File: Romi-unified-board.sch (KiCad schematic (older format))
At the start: 67 parts, among them J1 ServoAnalog, J10 LIDAR_DATA, J11 LIDAR_MOTOR, J12 ROMI-Encoder, J13 ROMI-Encoder, J14 THING, J15 THING, J2 Conn_01x19_Female, J3 LineSensor, J4 LineSensor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

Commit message: Re-routed board
Resolved issues #6  and #5
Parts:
- removed JP1: Jumper_3_Bridged12, Jumper:SolderJumper-3_P1.3mm_Bridged12_RoundedPad1.0x1.5mm, symbol Jumper:Jumper_3_Bridged12
- added SW2: SW_SPDT, unified:CSS-1210TB, symbol Switch:SW_SPDT
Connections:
- wire segments 277 -> 274
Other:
- moved on the sheet: H1
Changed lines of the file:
@@
 Text Notes 12250 5350 0    50   ~ 0
 ML-
-Text GLabel 4650 2050 2    50   Input ~ 0
+Text GLabel 4650 2350 2    50   Input ~ 0
 GPIO21
-Text GLabel 4650 2150 2    50   Input ~ 0
+Text GLabel 4650 2450 2    50   Input ~ 0
 GPIO17
-Text GLabel 4650 2250 2    50   Input ~ 0
+Text GLabel 4650 2550 2    50   Input ~ 0
 GPIO16
-Text GLabel 4650 2350 2    50   Input ~ 0
+Text GLabel 4650 2650 2    50   Input ~ 0
 GPIO19
-Text GLabel 4650 2450 2    50   Input ~ 0
+Text GLabel 4650 2750 2    50   Input ~ 0
 GPIO18
-Text GLabel 4650 2550 2    50   Input ~ 0
+Text GLabel 4650 2850 2    50   Input ~ 0
 GPIO5
-Text GLabel 4650 2650 2    50   Input ~ 0
+Text GLabel 4650 2950 2    50   Input ~ 0
 GPIO4
-Text GLabel 4650 2750 2    50   Input ~ 0
+Text GLabel 4650 3050 2    50   Input ~ 0
 GPIO36
-Text GLabel 4650 2850 2    50   Input ~ 0
+Text GLabel 4650 3150 2    50   Input ~ 0
 GPIO39
-Text GLabel 4650 2950 2    50   Input ~ 0
+Text GLabel 4650 3250 2    50   Input ~ 0
 GPIO34
-Text GLabel 4650 3050 2    50   Input ~ 0
+Text GLabel 4650 3350 2    50   Input ~ 0
 GPIO25
-Text GLabel 4650 3150 2    50   Input ~ 0
+Text GLabel 4650 3450 2    50   Input ~ 0
 GPIO26
 $Comp
 L power:GND #PWR0110
 U 1 1 5EEB6068
-P 4950 3250
-F 0 "#PWR0110" H 4950 3000 50  0001 C CNN
-F 1 "GND" V 4955 3122 50  0000 R CNN
-F 2 "" H 4950 3250 50  0001 C CNN
-F 3 "" H 4950 3250 50  0001 C CNN
-	1    4950 3250
+P 4950 3550
+F 0 "#PWR0110" H 4950 3300 50  0001 C CNN
+F 1 "GND" V 4955 3422 50  0000 R CNN
+F 2 "" H 4950 3550 50  0001 C CNN
+F 3 "" H 4950 3550 50  0001 C CNN
+	1    4950 3550
 	0    -1   -1   0
 $EndComp
@@
 L power:+3.3V #PWR0111
 U 1 1 5EEB70F6
-P 4950 3450
-F 0 "#PWR0111" H 4950 3300 50  0001 C CNN
-F 1 "+3.3V" V 4965 3578 50  0000 L CNN
-F 2 "" H 4950 3450 50  0001 C CNN
-F 3 "" H 4950 3450 50  0001 C CNN
-	1    4950 3450
+P 4950 3750
+F 0 "#PWR0111" H 4950 3600 50  0001 C CNN
+F 1 "+3.3V" V 4965 3878 50  0000 L CNN
+F 2 "" H 4950 3750 50  0001 C CNN
+F 3 "" H 4950 3750 50  0001 C CNN
+	1    4950 3750
 	0    1    1    0
 $EndComp
@@
 	2650 2850 2550 2850
 Wire Wire Line
-	4550 2050 4650 2050
-Wire Wire Line
-	4550 2150 4650 2150
-Wire Wire Line
-	4550 2250 4650 2250
-Wire Wire Line
 	4550 2350 4650 2350
 Wire Wire Line
@@
 	4550 3150 4650 3150
 Wire Wire Line
-	4950 3250 4550 3250
-Wire Wire Line
-	4550 3450 4950 3450
+	4550 3250 4650 3250
+Wire Wire Line
+	4550 3350 4650 3350
+Wire Wire Line
+	4550 3450 4650 3450
+Wire Wire Line
+	4950 3550 4550 3550
+Wire Wire Line
+	4550 3750 4950 3750
 $Comp
 L power:GND #PWR0113
@@
 Wire Wire Line
 	6300 1300 6350 1300
-$Comp
-L Mechanical:MountingHole H1
-U 1 1 5EF4C315
-P 5200 3850
-F 0 "H1" H 5300 3896 50  0000 L CNN
-F 1 "MountingHole" H 5300 3805 50  0000 L CNN
-F 2 "MountingHole:MountingHole_2.2mm_M2_DIN965" H 5200 3850 50  0001 C CNN
-F 3 "~" H 5200 3850 50  0001 C CNN
-	1    5200 3850
-	1    0    0    -1
-$EndComp
 $Comp
 L Mechanical:MountingHole H2
@@
 NoConn ~ 1250 2450
 NoConn ~ 2150 2550
-NoConn ~ 5050 2950
+NoConn ~ 5050 3250
 NoConn ~ 1250 2250
 NoConn ~ 1250 2300
-NoConn ~ 5050 2750
-NoConn ~ 5050 2850
+NoConn ~ 5050 3050
+NoConn ~ 5050 3150
 NoConn ~ 2150 2250
 NoConn ~ 2150 2350
@@
 NoConn ~ 3550 3050
 NoConn ~ 3550 3150
-NoConn ~ 5050 2150
-NoConn ~ 5050 2250
+NoConn ~ 5050 2450
+NoConn ~ 5050 2550
 NoConn ~ 1250 3050
 NoConn ~ 1250 2950
 NoConn ~ 2150 2650
-NoConn ~ 5050 3150
-NoConn ~ 5050 2650
+NoConn ~ 5050 3450
+NoConn ~ 5050 2950
 NoConn ~ 2150 2850
 NoConn ~ 3550 3250
-NoConn ~ 5050 3050
+NoConn ~ 5050 3350
 NoConn ~ 2150 2750
 NoConn ~ 3550 3550
@@
 Text Notes 8650 2900 0    50   ~ 0
 Free: 23 22 21 19 18 5
-Text GLabel 3200 6550 0    50   Input ~ 0
+Text GLabel 3650 7050 2    50   Input ~ 0
 GPIO23
-Text GLabel 3800 6550 2    50   Input ~ 0
+Text GLabel 3650 7250 2    50   Input ~ 0
 GPIO21
 $Comp
@@
 Wire Wire Line
 	6000 -850 6000 -800
-$Comp
-L Jumper:Jumper_3_Bridged12 JP1
-U 1 1 5F229CDD
-P 3500 6550
-F 0 "JP1" H 3500 6754 50  0000 C CNN
-F 1 "Jumper_3_Bridged12" H 3500 6663 50  0000 C CNN
-F 2 "Jumper:SolderJumper-3_P1.3mm_Bridged12_RoundedPad1.0x1.5mm" H 3500 6550 50  0001 C CNN
-F 3 "~" H 3500 6550 50  0001 C CNN
-	1    3500 6550
-	-1   0    0    1
-$EndComp
-Wire Wire Line
-	3800 6550 3750 6550
-Wire Wire Line
-	3500 6700 3500 6750
-Wire Wire Line
-	3250 6550 3200 6550
 Text GLabel 6350 1000 2    50   Input ~ 0
 GPIO23
 Text GLabel 8000 1300 2    50   Input ~ 0
 SDA
-Text GLabel 3500 6400 1    50   Input ~ 0
+Text GLabel 3250 7150 0    50   Input ~ 0
 SDA
 $Comp
@@
 Wire Wire Line
 	6400 2650 6300 2650
+$Comp
+L Mechanical:MountingHole H1
+U 1 1 5EF4C315
+P 5550 4000
+F 0 "H1" H 5650 4046 50  0000 L CNN
+F 1 "MountingHole" H 5750 3900 50  0000 L CNN
+F 2 "MountingHole:MountingHole_2.2mm_M2_DIN965" H 5550 4000 50  0001 C CNN
+F 3 "~" H 5550 4000 50  0001 C CNN
+	1    5550 4000
+	1    0    0    -1
+$EndComp
+$Comp
+L Switch:SW_SPDT SW2
+U 1 1 5F890447
+P 3450 7150
+F 0 "SW2" H 3450 7435 50  0000 C CNN
+F 1 "SW_SPDT" H 3450 7344 50  0000 C CNN
+F 2 "unified:CSS-1210TB" H 3450 7150 50  0001 C CNN
+F 3 "~" H 3450 7150 50  0001 C CNN
+	1    3450 7150
+	1    0    0    -1
+$EndComp
 $EndSCHEMATC

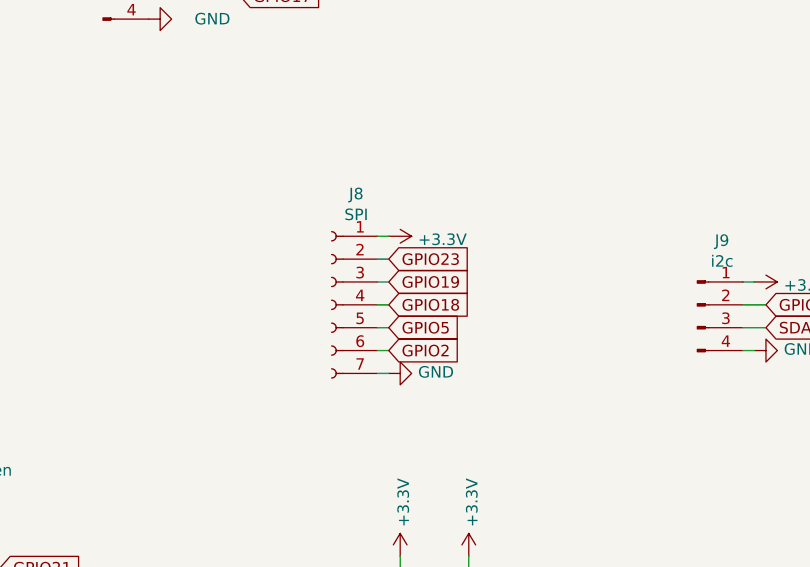
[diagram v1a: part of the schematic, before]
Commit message: flipped ultrasonic, removed IO2 from j8
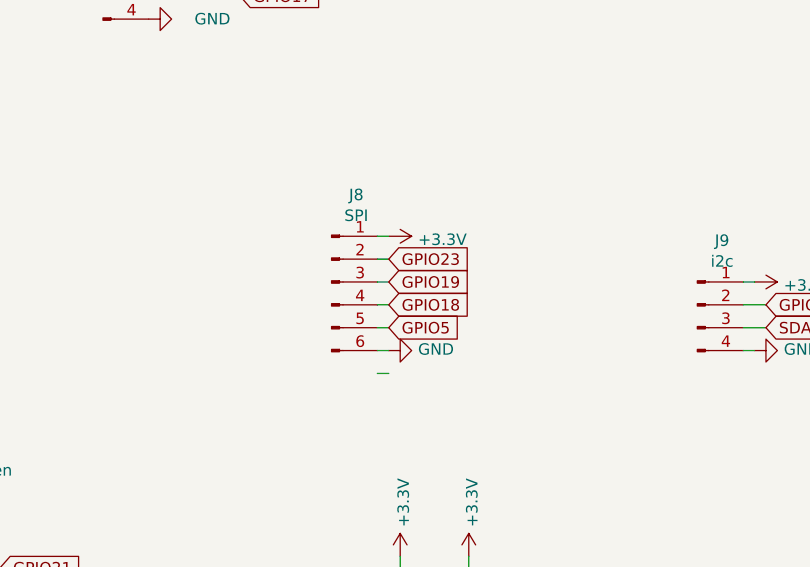
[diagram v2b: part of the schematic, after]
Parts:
- removed J8: SPI, Connector_PinSocket_2.54mm:PinSocket_1x07_P2.54mm_Vertical, symbol Connector:Conn_01x07_Female
- added J8: SPI, Connector_PinSocket_2.54mm:PinSocket_1x06_P2.54mm_Vertical, symbol Connector:Conn_01x06_Male
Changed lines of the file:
@@
 L power:GND #PWR0123
 U 1 1 5EEAECD4
-P 6350 1500
-F 0 "#PWR0123" H 6350 1250 50  0001 C CNN
-F 1 "GND" V 6355 1372 50  0000 R CNN
-F 2 "" H 6350 1500 50  0001 C CNN
-F 3 "" H 6350 1500 50  0001 C CNN
-	1    6350 1500
+P 6350 1400
+F 0 "#PWR0123" H 6350 1150 50  0001 C CNN
+F 1 "GND" V 6355 1272 50  0000 R CNN
+F 2 "" H 6350 1400 50  0001 C CNN
+F 3 "" H 6350 1400 50  0001 C CNN
+	1    6350 1400
 	0    -1   -1   0
 $EndComp
@@
 Text GLabel 16750 2800 0    50   Input ~ 0
 GPIO15
-$Comp
-L Connector:Conn_01x07_Female J8
-U 1 1 5F79F56E
-P 6100 1200
-F 0 "J8" H 5992 1685 50  0000 C CNN
-F 1 "SPI" H 5992 1594 50  0000 C CNN
-F 2 "Connector_PinSocket_2.54mm:PinSocket_1x07_P2.54mm_Vertical" H 6100 1200 50  0001 C CNN
-F 3 "~" H 6100 1200 50  0001 C CNN
-	1    6100 1200
-	-1   0    0    -1
-$EndComp
-Text GLabel 6350 1400 2    50   Input ~ 0
-GPIO2
 Wire Wire Line
 	6350 1500 6300 1500
@@
 	1    0    0    -1
 $EndComp
+$Comp
+L Connector:Conn_01x06_Male J8
+U 1 1 5F879B4D
+P 6100 1100
+F 0 "J8" H 6208 1481 50  0000 C CNN
+F 1 "SPI" H 6208 1390 50  0000 C CNN
+F 2 "Connector_PinSocket_2.54mm:PinSocket_1x06_P2.54mm_Vertical" H 6100 1100 50  0001 C CNN
+F 3 "~" H 6100 1100 50  0001 C CNN
+	1    6100 1100
+	1    0    0    -1
+$EndComp

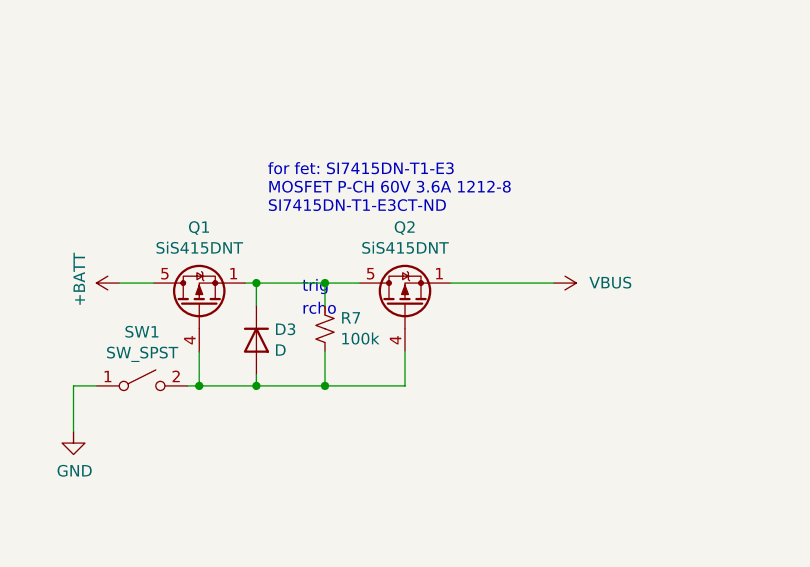
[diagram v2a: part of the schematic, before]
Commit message: Changes for rev2
rotated Q2
Fixed too-thin trace in DC-DC Circuit.
Created correct footprint for U1. No 9th pad.
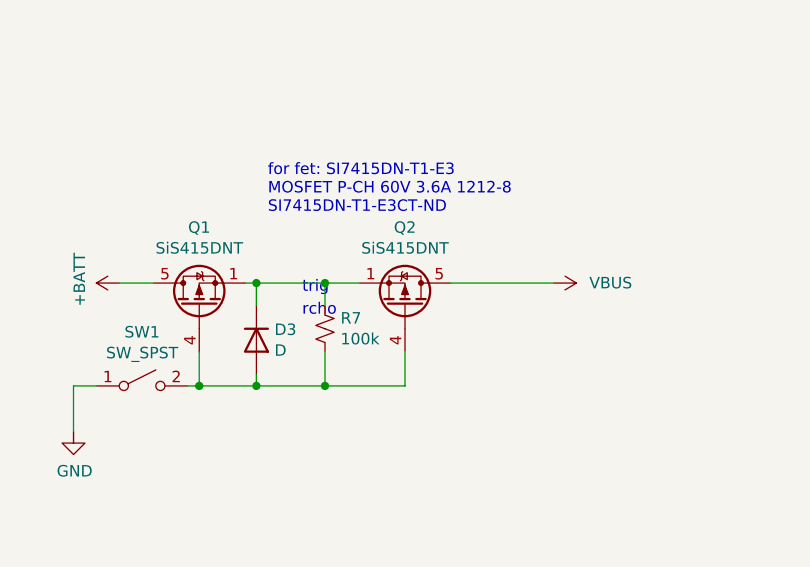
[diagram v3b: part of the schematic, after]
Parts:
- U1: footprint Package_DFN_QFN:DFN-8-1EP_3x3mm_P0.65mm_EP1.7x2.05mm -> unified:MP4423H
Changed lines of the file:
@@
 F 3 "https://www.vishay.com/docs/63684/sis415dnt.pdf" V 9100 -1100 50  0001 L CNN
 	1    9100 -1100
-	0    -1   -1   0
+	0    1    -1   0
 $EndComp
 $Comp
@@
 F 0 "U1" H 7350 5565 50  0000 C CNN
 F 1 "MP4423H" H 7350 5474 50  0000 C CNN
-F 2 "Package_DFN_QFN:DFN-8-1EP_3x3mm_P0.65mm_EP1.7x2.05mm" H 7050 4250 50  0001 C CNN
+F 2 "unified:MP4423H" H 7050 4250 50  0001 C CNN
 F 3 "" H 7050 4250 50  0001 C CNN
 	1    7350 4900

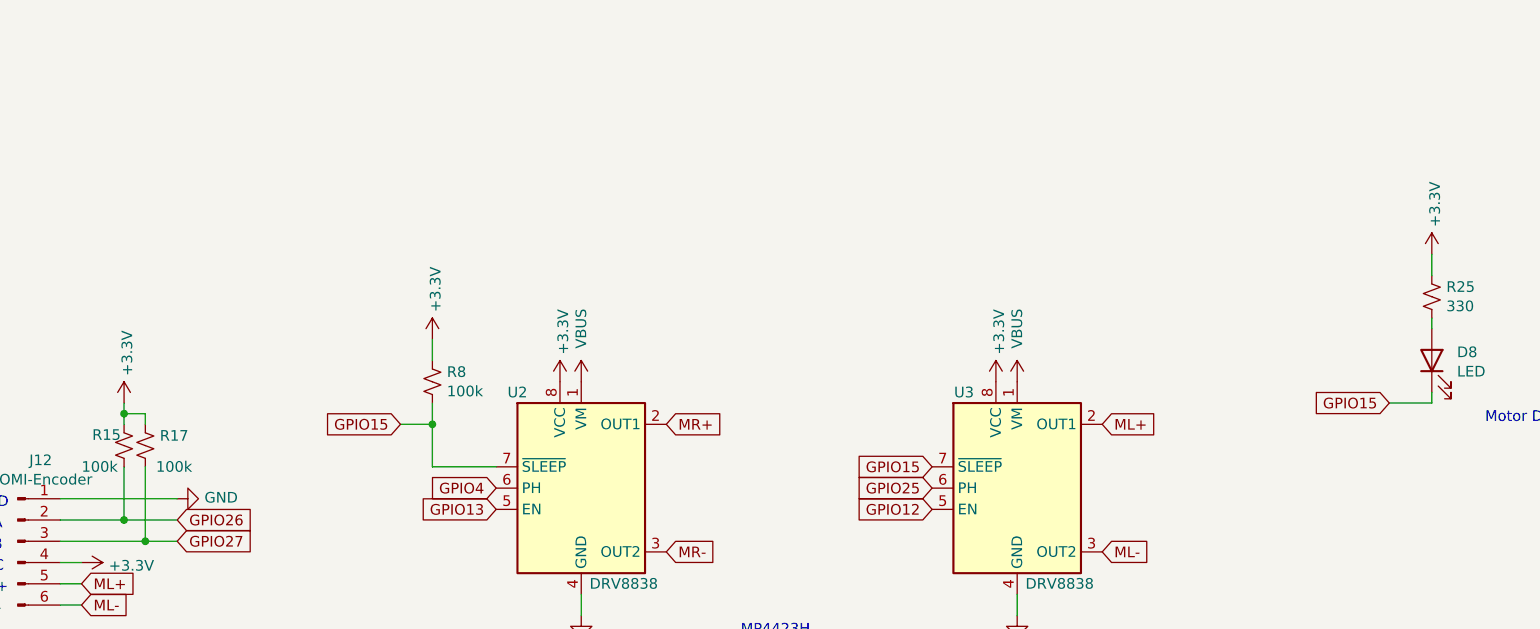
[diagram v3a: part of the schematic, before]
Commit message: Motor Disable is now a physical switch.
#7
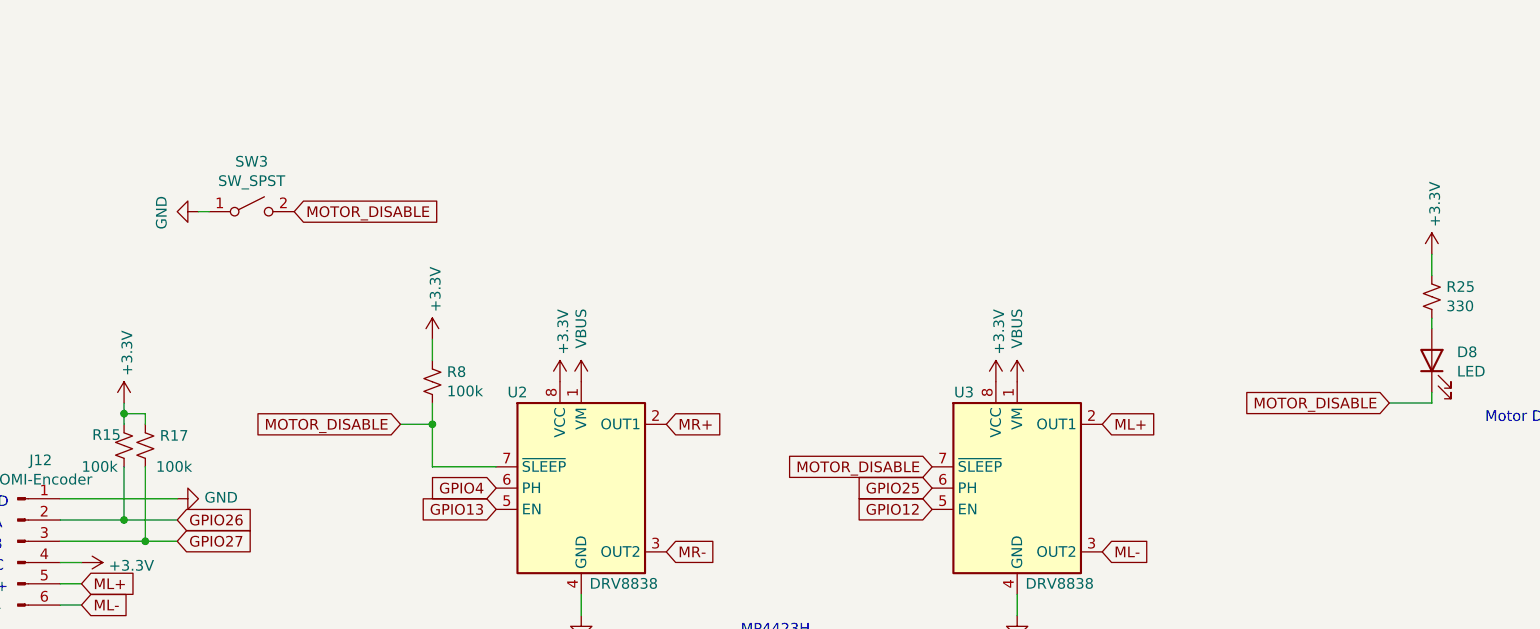
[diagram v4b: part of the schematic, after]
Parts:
- added SW3: SW_SPST, unified:CSS-1210TB, symbol Switch:SW_SPST
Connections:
- net labels added: MOTOR_DISABLE
- wire segments 274 -> 275
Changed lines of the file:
@@
 $EndComp
 Text GLabel 14250 2600 0    50   Input ~ 0
-GPIO15
+MOTOR_DISABLE
 Text GLabel 6350 1100 2    50   Input ~ 0
 GPIO19
@@
 	14400 2500 14400 2600
 Connection ~ 14400 2600
-Text GLabel 16750 2800 0    50   Input ~ 0
-GPIO15
 Wire Wire Line
 	6350 1500 6300 1500
@@
 Text Notes 17100 150  0    50   ~ 0
 DNP U5,U6,U7,U4
-Text GLabel 18900 2500 0    50   Input ~ 0
-GPIO15
 $Comp
 L Device:LED D8
@@
 	1    0    0    -1
 $EndComp
+Text GLabel 16750 2800 0    50   Input ~ 0
+MOTOR_DISABLE
+$Comp
+L Switch:SW_SPST SW3
+U 1 1 5F9B53FD
+P 13550 1600
+F 0 "SW3" H 13550 1835 50  0000 C CNN
+F 1 "SW_SPST" H 13550 1744 50  0000 C CNN
+F 2 "unified:CSS-1210TB" H 13550 1600 50  0001 C CNN
+F 3 "~" H 13550 1600 50  0001 C CNN
+	1    13550 1600
+	1    0    0    -1
+$EndComp
+Text GLabel 13750 1600 2    50   Input ~ 0
+MOTOR_DISABLE
+$Comp
+L power:GND #PWR0144
+U 1 1 5F9B5F0A
+P 13300 1600
+F 0 "#PWR0144" H 13300 1350 50  0001 C CNN
+F 1 "GND" H 13305 1427 50  0000 C CNN
+F 2 "" H 13300 1600 50  0001 C CNN
+F 3 "" H 13300 1600 50  0001 C CNN
+	1    13300 1600
+	0    1    1    0
+$EndComp
+Wire Wire Line
+	13350 1600 13300 1600
+Text GLabel 18900 2500 0    50   Input ~ 0
+MOTOR_DISABLE
 $EndSCHEMATC

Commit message: Rev2
Added smart servo connectors
Added IR sensor
Updated silk label
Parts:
- added C16, C17: 220u, Capacitor_SMD:CP_Elec_6.3x3.9, symbol Device:CP
- added J16, J17, J18: Conn_01x03_Male, Connector_JST:JST_PH_B3B-PH-K_1x03_P2.00mm_Vertical, symbol Connector:Conn_01x03_Male
- added U4: TSSP58038, OptoDevice:Vishay_MINICAST-3Pin, symbol Sensor_Proximity:TSSP58038
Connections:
- wire segments 275 -> 279
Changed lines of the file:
@@
 Text GLabel 18900 2500 0    50   Input ~ 0
 MOTOR_DISABLE
+$Comp
+L Connector:Conn_01x03_Male J16
+U 1 1 5F9C6157
+P 13550 450
+F 0 "J16" H 13658 731 50  0000 C CNN
+F 1 "Conn_01x03_Male" H 13658 640 50  0000 C CNN
+F 2 "Connector_JST:JST_PH_B3B-PH-K_1x03_P2.00mm_Vertical" H 13550 450 50  0001 C CNN
+F 3 "~" H 13550 450 50  0001 C CNN
+	1    13550 450
+	1    0    0    -1
+$EndComp
+$Comp
+L power:GND #PWR0147
+U 1 1 5F9C7080
+P 13750 350
+F 0 "#PWR0147" H 13750 100 50  0001 C CNN
+F 1 "GND" H 13755 177 50  0000 C CNN
+F 2 "" H 13750 350 50  0001 C CNN
+F 3 "" H 13750 350 50  0001 C CNN
+	1    13750 350
+	0    -1   -1   0
+$EndComp
+Text GLabel 13750 550  2    50   Input ~ 0
+GPIO33
+$Comp
+L power:VBUS #PWR0148
+U 1 1 5F9C76D4
+P 13750 450
+F 0 "#PWR0148" H 13750 300 50  0001 C CNN
+F 1 "VBUS" V 13750 700 50  0000 C CNN
+F 2 "" H 13750 450 50  0001 C CNN
+F 3 "" H 13750 450 50  0001 C CNN
+	1    13750 450
+	0    1    1    0
+$EndComp
+$Comp
+L Connector:Conn_01x03_Male J17
+U 1 1 5F9C9712
+P 14400 450
+F 0 "J17" H 14508 731 50  0000 C CNN
+F 1 "Conn_01x03_Male" H 14508 640 50  0000 C CNN
+F 2 "Connector_JST:JST_PH_B3B-PH-K_1x03_P2.00mm_Vertical" H 14400 450 50  0001 C CNN
+F 3 "~" H 14400 450 50  0001 C CNN
+	1    14400 450
+	1    0    0    -1
+$EndComp
+$Comp
+L power:GND #PWR0149
+U 1 1 5F9C9718
+P 14600 350
+F 0 "#PWR0149" H 14600 100 50  0001 C CNN
+F 1 "GND" H 14605 177 50  0000 C CNN
+F 2 "" H 14600 350 50  0001 C CNN
+F 3 "" H 14600 350 50  0001 C CNN
+	1    14600 350
+	0    -1   -1   0
+$EndComp
+Text GLabel 14600 550  2    50   Input ~ 0
+GPIO33
+$Comp
+L power:VBUS #PWR0150
+U 1 1 5F9C971F
+P 14600 450
+F 0 "#PWR0150" H 14600 300 50  0001 C CNN
+F 1 "VBUS" V 14600 700 50  0000 C CNN
+F 2 "" H 14600 450 50  0001 C CNN
+F 3 "" H 14600 450 50  0001 C CNN
+	1    14600 450
+	0    1    1    0
+$EndComp
+$Comp
+L Connector:Conn_01x03_Male J18
+U 1 1 5F9E0D75
+P 15200 450
+F 0 "J18" H 15308 731 50  0000 C CNN
+F 1 "Conn_01x03_Male" H 15308 640 50  0000 C CNN
+F 2 "Connector_JST:JST_PH_B3B-PH-K_1x03_P2.00mm_Vertical" H 15200 450 50  0001 C CNN
+F 3 "~" H 15200 450 50  0001 C CNN
+	1    15200 450
+	1    0    0    -1
+$EndComp
+$Comp
+L power:GND #PWR0151
+U 1 1 5F9E0D7B
+P 15400 350
+F 0 "#PWR0151" H 15400 100 50  0001 C CNN
+F 1 "GND" H 15405 177 50  0000 C CNN
+F 2 "" H 15400 350 50  0001 C CNN
+F 3 "" H 15400 350 50  0001 C CNN
+	1    15400 350
+	0    -1   -1   0
+$EndComp
+Text GLabel 15400 550  2    50   Input ~ 0
+GPIO33
+$Comp
+L power:VBUS #PWR0154
+U 1 1 5F9E0D82
+P 15400 450
+F 0 "#PWR0154" H 15400 300 50  0001 C CNN
+F 1 "VBUS" V 15400 700 50  0000 C CNN
+F 2 "" H 15400 450 50  0001 C CNN
+F 3 "" H 15400 450 50  0001 C CNN
+	1    15400 450
+	0    1    1    0
+$EndComp
+$Comp
+L Device:CP C17
+U 1 1 5F9C77ED
+P 12400 400
+F 0 "C17" H 12518 446 50  0000 L CNN
+F 1 "220u" H 12518 355 50  0000 L CNN
+F 2 "Capacitor_SMD:CP_Elec_6.3x3.9" H 12438 250 50  0001 C CNN
+F 3 "~" H 12400 400 50  0001 C CNN
+	1    12400 400
+	1    0    0    -1
+$EndComp
+$Comp
+L Device:CP C16
+U 1 1 5F9C873E
+P 12050 400
+F 0 "C16" H 12168 446 50  0000 L CNN
+F 1 "220u" H 12168 355 50  0000 L CNN
+F 2 "Capacitor_SMD:CP_Elec_6.3x3.9" H 12088 250 50  0001 C CNN
+F 3 "~" H 12050 400 50  0001 C CNN
+	1    12050 400
+	1    0    0    -1
+$EndComp
+$Comp
+L power:VBUS #PWR0155
+U 1 1 5F9C8DC0
+P 12050 250
+F 0 "#PWR0155" H 12050 100 50  0001 C CNN
+F 1 "VBUS" V 12050 500 50  0000 C CNN
+F 2 "" H 12050 250 50  0001 C CNN
+F 3 "" H 12050 250 50  0001 C CNN
+	1    12050 250
+	1    0    0    -1
+$EndComp
+$Comp
+L power:VBUS #PWR0156
+U 1 1 5F9C973B
+P 12400 250
+F 0 "#PWR0156" H 12400 100 50  0001 C CNN
+F 1 "VBUS" V 12400 500 50  0000 C CNN
+F 2 "" H 12400 250 50  0001 C CNN
+F 3 "" H 12400 250 50  0001 C CNN
+	1    12400 250
+	1    0    0    -1
+$EndComp
+$Comp
+L power:GND #PWR0157
+U 1 1 5F9C9CDB
+P 12050 550
+F 0 "#PWR0157" H 12050 300 50  0001 C CNN
+F 1 "GND" H 12055 377 50  0000 C CNN
+F 2 "" H 12050 550 50  0001 C CNN
+F 3 "" H 12050 550 50  0001 C CNN
+	1    12050 550
+	1    0    0    -1
+$EndComp
+$Comp
+L power:GND #PWR0158
+U 1 1 5F9CA263
+P 12400 550
+F 0 "#PWR0158" H 12400 300 50  0001 C CNN
+F 1 "GND" H 12405 377 50  0000 C CNN
+F 2 "" H 12400 550 50  0001 C CNN
+F 3 "" H 12400 550 50  0001 C CNN
+	1    12400 550
+	1    0    0    -1
+$EndComp
+$Comp
+L Sensor_Proximity:TSSP58038 U4
+U 1 1 5FA17FA5
+P 2200 -650
+F 0 "U4" H 2188 -225 50  0000 C CNN
+F 1 "TSSP58038" H 2188 -316 50  0000 C CNN
+F 2 "OptoDevice:Vishay_MINICAST-3Pin" H 2150 -1025 50  0001 C CNN
+F 3 "http://www.vishay.com/docs/82476/tssp58p38.pdf" H 2850 -350 50  0001 C CNN
+	1    2200 -650
+	1    0    0    -1
+$EndComp
+Text GLabel 2750 -650 2    50   Input ~ 0
+GPIO15
+$Comp
+L power:+3.3V #PWR0159
+U 1 1 5FA1A71A
+P 2750 -900
+F 0 "#PWR0159" H 2750 -1050 50  0001 C CNN
+F 1 "+3.3V" V 2765 -772 50  0000 L CNN
+F 2 "" H 2750 -900 50  0001 C CNN
+F 3 "" H 2750 -900 50  0001 C CNN
+	1    2750 -900
+	1    0    0    -1
+$EndComp
+$Comp
+L power:GND #PWR0161
+U 1 1 5FA1B4BD
+P 2750 -450
+F 0 "#PWR0161" H 2750 -700 50  0001 C CNN
+F 1 "GND" V 2750 -650 50  0000 R CNN
+F 2 "" H 2750 -450 50  0001 C CNN
+F 3 "" H 2750 -450 50  0001 C CNN
+	1    2750 -450
+	0    -1   -1   0
+$EndComp
+Wire Wire Line
+	2600 -850 2750 -850
+Wire Wire Line
+	2750 -850 2750 -900
+Wire Wire Line
+	2750 -650 2600 -650
+Wire Wire Line
+	2750 -450 2600 -450
 $EndSCHEMATC
